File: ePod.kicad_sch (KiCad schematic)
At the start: 0 parts

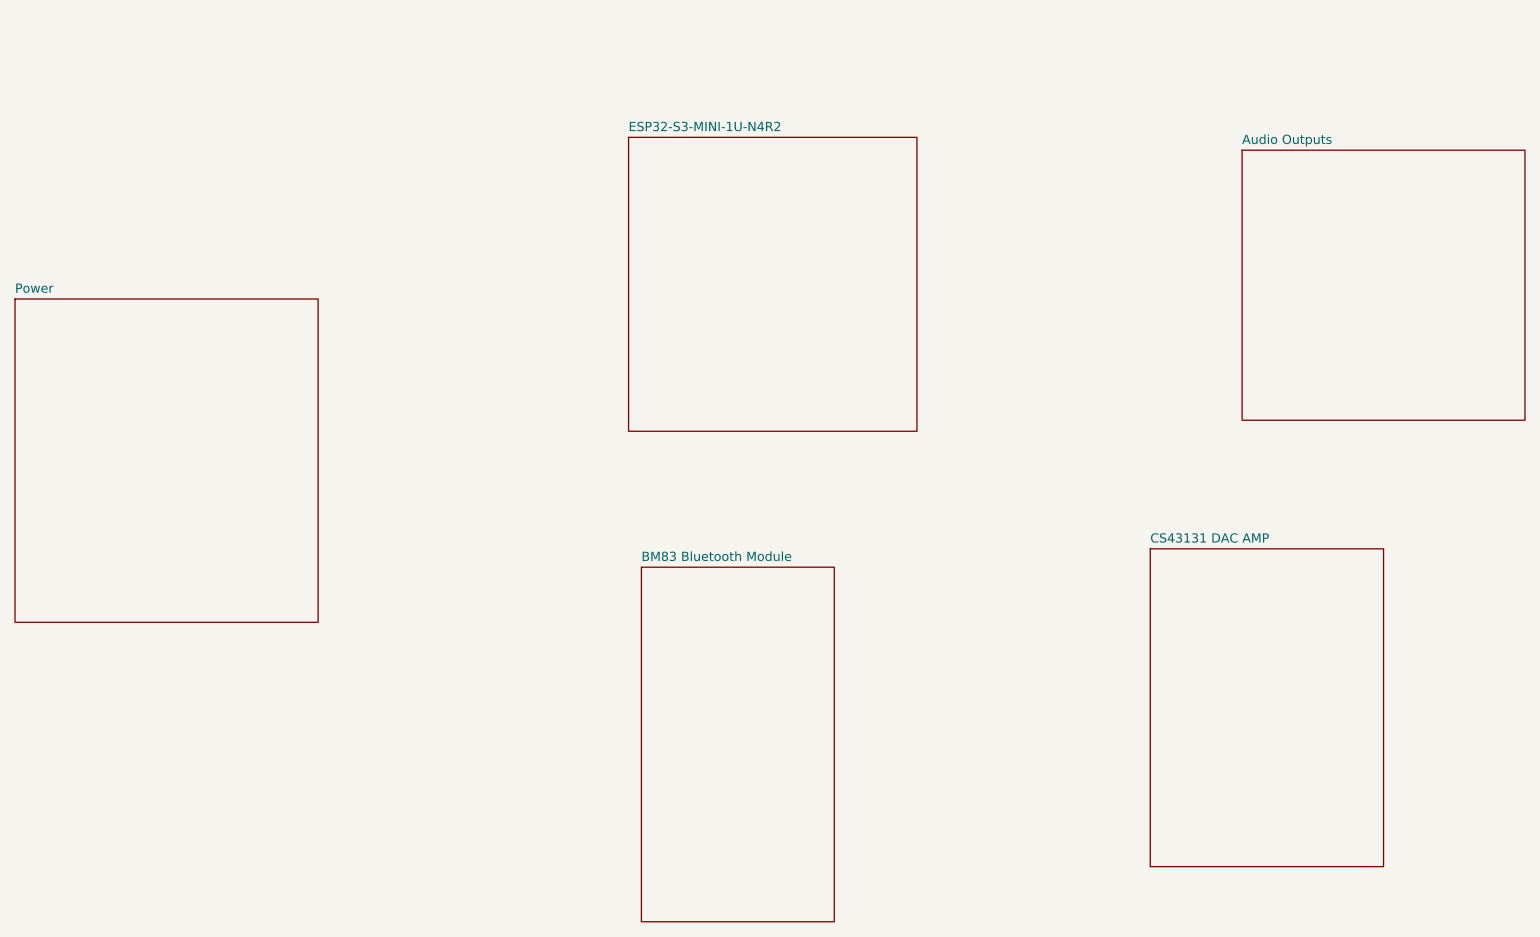
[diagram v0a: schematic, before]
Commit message: Initial design of CS43131 and level shifters
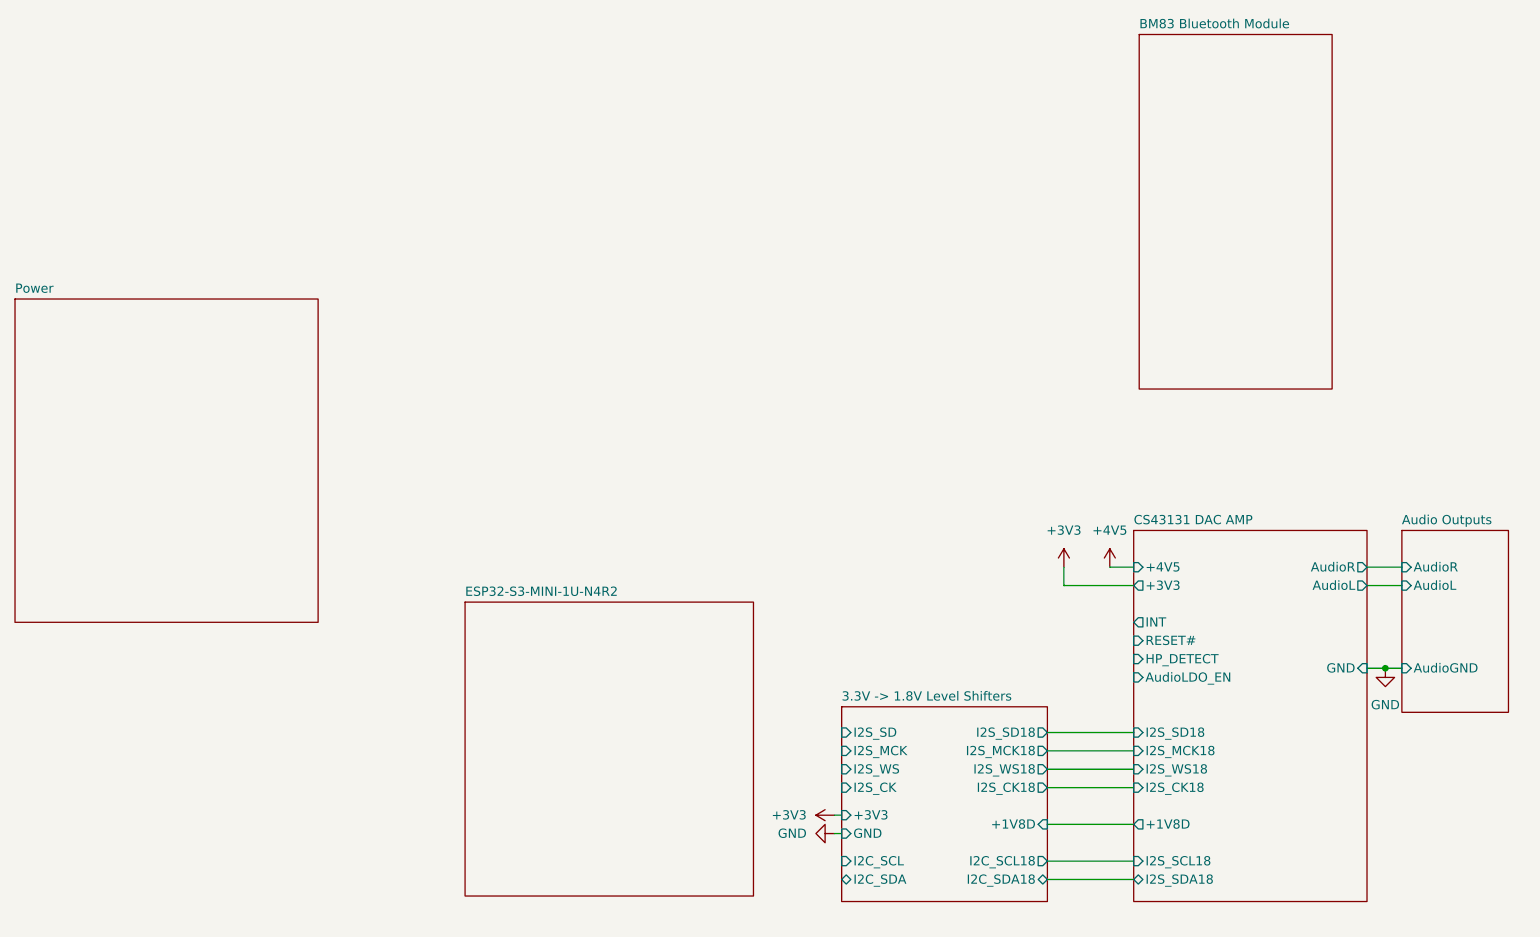
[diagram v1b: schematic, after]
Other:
- added sheet 3.3V -> 1.8V Level Shifters (level_shifters.kicad_sch)
- sheet Audio Outputs ports: added AudioGND, AudioL, AudioR; removed none
- sheet CS43131 DAC AMP ports: added +1V8D, +3V3, +4V5, AudioL, AudioLDO_EN, AudioR, GND, HP_DETECT, I2S_CK18, I2S_MCK18, I2S_SCL18, I2S_SD18, I2S_SDA18, I2S_WS18, INT, RESET#; removed none
